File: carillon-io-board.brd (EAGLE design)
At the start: 111.7 x 96.2 mm, 51 parts, among them J1 22-27-2031-03, J10 22-27-2031-03, J2 22-27-2031-03, J3 22-27-2031-03, J4 22-27-2031-03, J5 22-27-2031-03, J6 22-27-2031-03, J7 22-27-2031-03, J8 22-27-2031-03, J9 22-27-2031-03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

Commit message: fix board
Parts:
- removed R10, R12, R14, R16, R18, R2, R20, R4, R6, R8: (no value), resistor:0207/10
- J1, J10, J2, J3, J4, J5, J6, J7, J8, J9: value 22-27-2031-03 -> 22-05-7048-04; device con-molex:6410-03 -> con-molex:7395-04
- moved R1 1.91 mm to (97.2, 63.5)
- moved R11 1.91 mm to (46.4, 63.5)
- moved R13 1.91 mm to (36.2, 63.5)
- moved R15 1.91 mm to (26.0, 63.5)
- moved R17 1.91 mm to (15.9, 63.5)
- moved R3 1.91 mm to (87.0, 63.5)
- moved R5 1.91 mm to (76.8, 63.5)
- moved R7 1.91 mm to (66.7, 63.5)
- moved R9 1.91 mm to (56.5, 63.5)
- moved R19 1.91 mm to (5.71, 63.5)
- moved J1 1.27 mm to (102.9, 83.8)
- moved J6 1.27 mm to (52.1, 83.8)
- moved J10 1.27 mm to (11.4, 83.8)
- moved J8 1.27 mm to (31.8, 83.8)
- moved J9 1.27 mm to (21.6, 83.8)
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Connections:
- net 12V: now also J1.2, J10.2, J2.2, J3.2, J4.2, J5.2, J6.2, J7.2, J8.2, J9.2; no longer J1.1, J10.1, J2.1, J3.1, J4.1, J5.1, J6.1, J7.1, J8.1, J9.1
- net GND: now also J1.1, J10.1, J2.1, J3.1, J4.1, J5.1, J6.1, J7.1, J8.1, J9.1; no longer R10.2, R12.2, R14.2, R16.2, R18.2, R2.2, R20.2, R4.2, R6.2, R8.2
- net IN1: now also J1.3; no longer J1.2, R2.1
- net IN10: now also J10.3; no longer J10.2, R20.1
- net IN2: now also J2.3; no longer J2.2, R4.1
- net IN3: now also J3.3; no longer J3.2, R6.1
- net IN4: now also J4.3; no longer J4.2, R8.1
- net IN5: now also J5.3; no longer J5.2, R10.1
- net IN6: now also J6.3; no longer J6.2, R12.1
- net IN7: now also J7.3; no longer J7.2, R14.1
- net IN8: now also J8.3; no longer J8.2, R16.1
- net IN9: now also J9.3; no longer J9.2, R18.1
- net N$1: now also J1.4; no longer J1.3
- net N$10: now also J10.4; no longer J10.3
- net N$2: now also J6.4; no longer J6.3
- net N$3: now also J2.4; no longer J2.3
- net N$4: now also J3.4; no longer J3.3
- net N$5: now also J4.4; no longer J4.3
- net N$6: now also J5.4; no longer J5.3
- net N$7: now also J7.4; no longer J7.3
- net N$8: now also J8.4; no longer J8.3
- net N$9: now also J9.4; no longer J9.3
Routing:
- net IN8: track 114.7 -> 112.3 mm
- net IN7: track 89.3 -> 86.9 mm
- net IN9: track 140.8 -> 138.5 mm
- net IN10: track 165.5 -> 163.1 mm
- net IN2: track 45.4 -> 43.5 mm
- net IN1: track 47.5 -> 45.6 mm
- net IN3: track 43.3 -> 41.4 mm
- net T2: track 6.61 -> 5.08 mm
- net T7: track 6.61 -> 5.08 mm
- net T5: track 6.61 -> 5.08 mm
- net T9: track 6.61 -> 5.08 mm
- net T8: track 6.61 -> 5.08 mm
- net T6: track 6.61 -> 5.08 mm
- net T4: track 6.61 -> 5.08 mm
- net T3: track 6.61 -> 5.08 mm
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
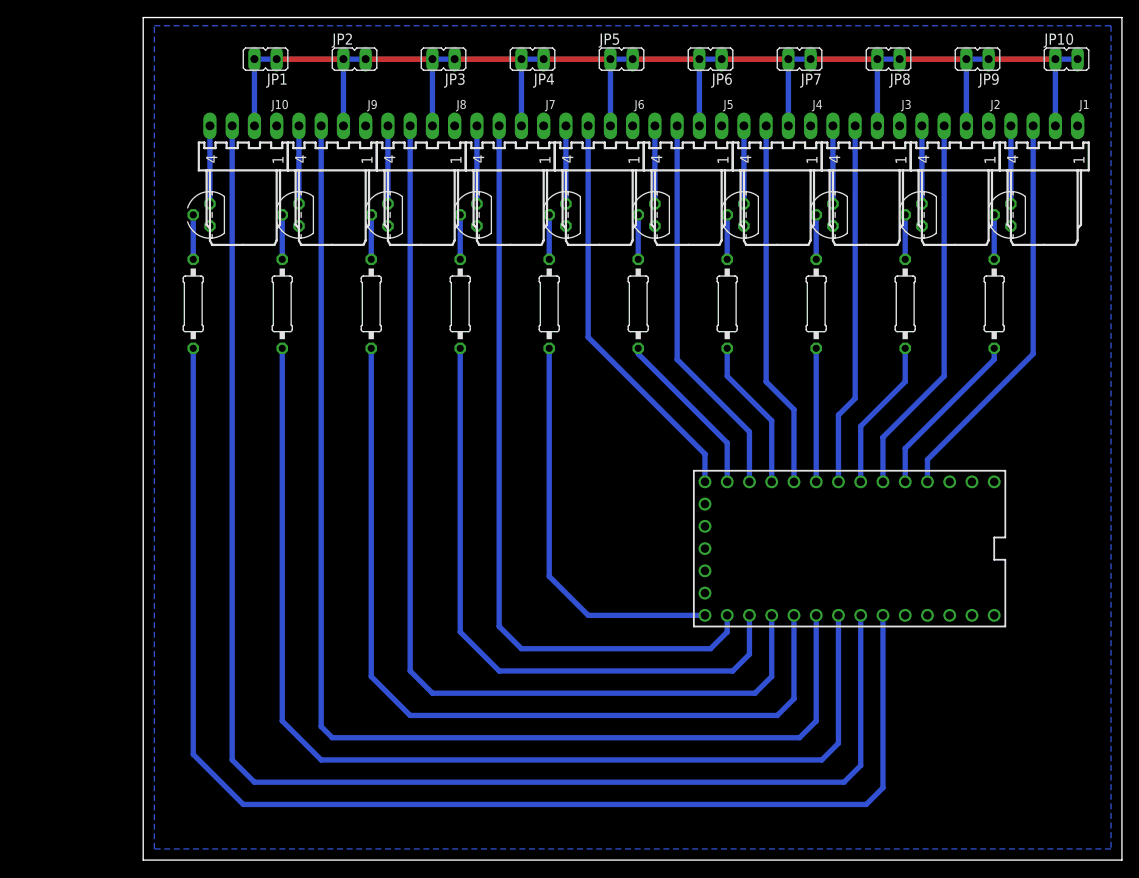
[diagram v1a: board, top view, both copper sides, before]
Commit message: io board proved, firmware file added
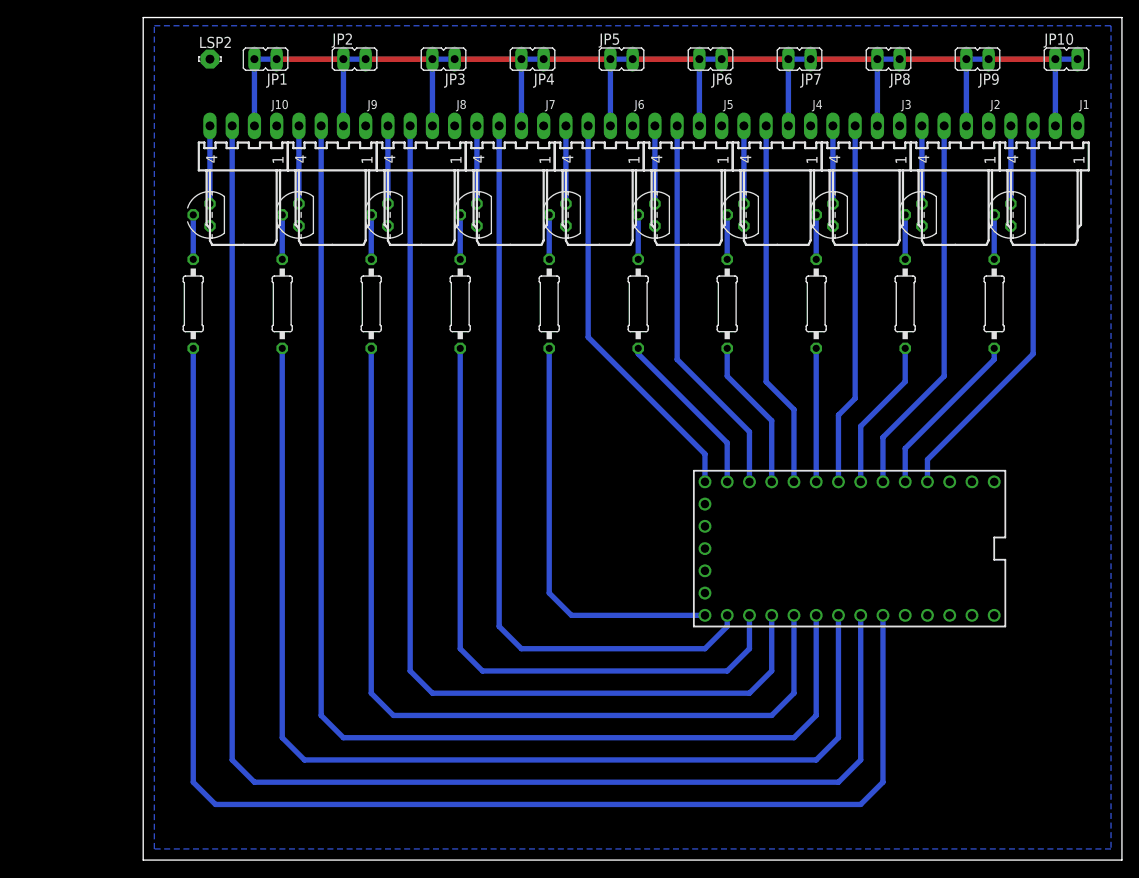
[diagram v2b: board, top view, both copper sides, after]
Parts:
- added LSP2: LSP10, solpad:LSP10
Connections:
- net GND: now also LSP2.MP
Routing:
- net OUT10: track 147.9 -> 149.4 mm
- net IN9: track 138.5 -> 137.4 mm
- net OUT6: track 45.7 -> 46.8 mm
- net OUT7: track 72.5 -> 73.2 mm
- net OUT9: track 123.3 -> 124.0 mm
- net OUT8: track 97.9 -> 98.6 mm
